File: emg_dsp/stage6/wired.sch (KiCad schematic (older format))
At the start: 51 parts, among them U38 OMNETICS_36, U41 MIC5365, U42 TC1016, U43 TC1016, U44 AD7980, U45 AD7980, U46 ADR381, U47 8X100, U48 8X100, U49 TC1016, U50 IL715-3, U51 DCP01DB, U52 IL715-3, U92 RHA2116, U93 RHA2116

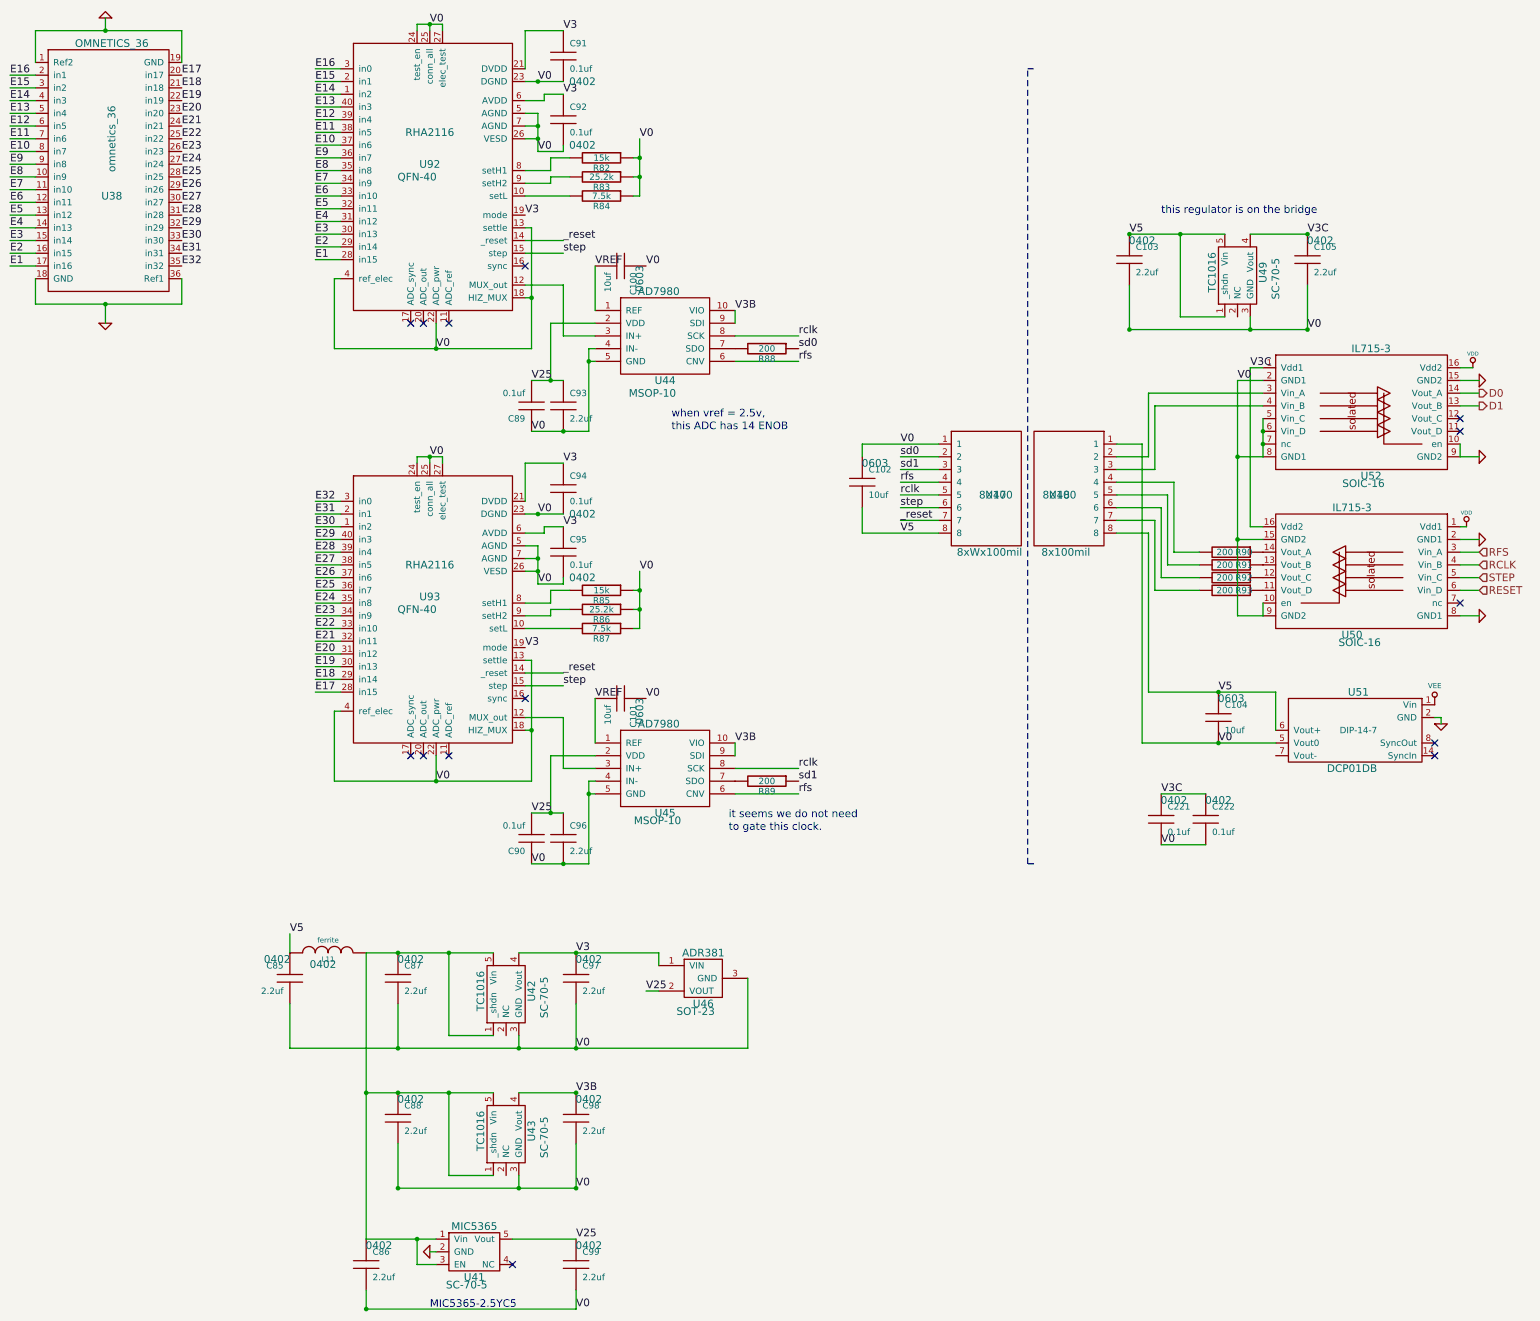
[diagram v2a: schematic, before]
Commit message: wired, wireless, some of bridge are routed. next up is the EMG system.
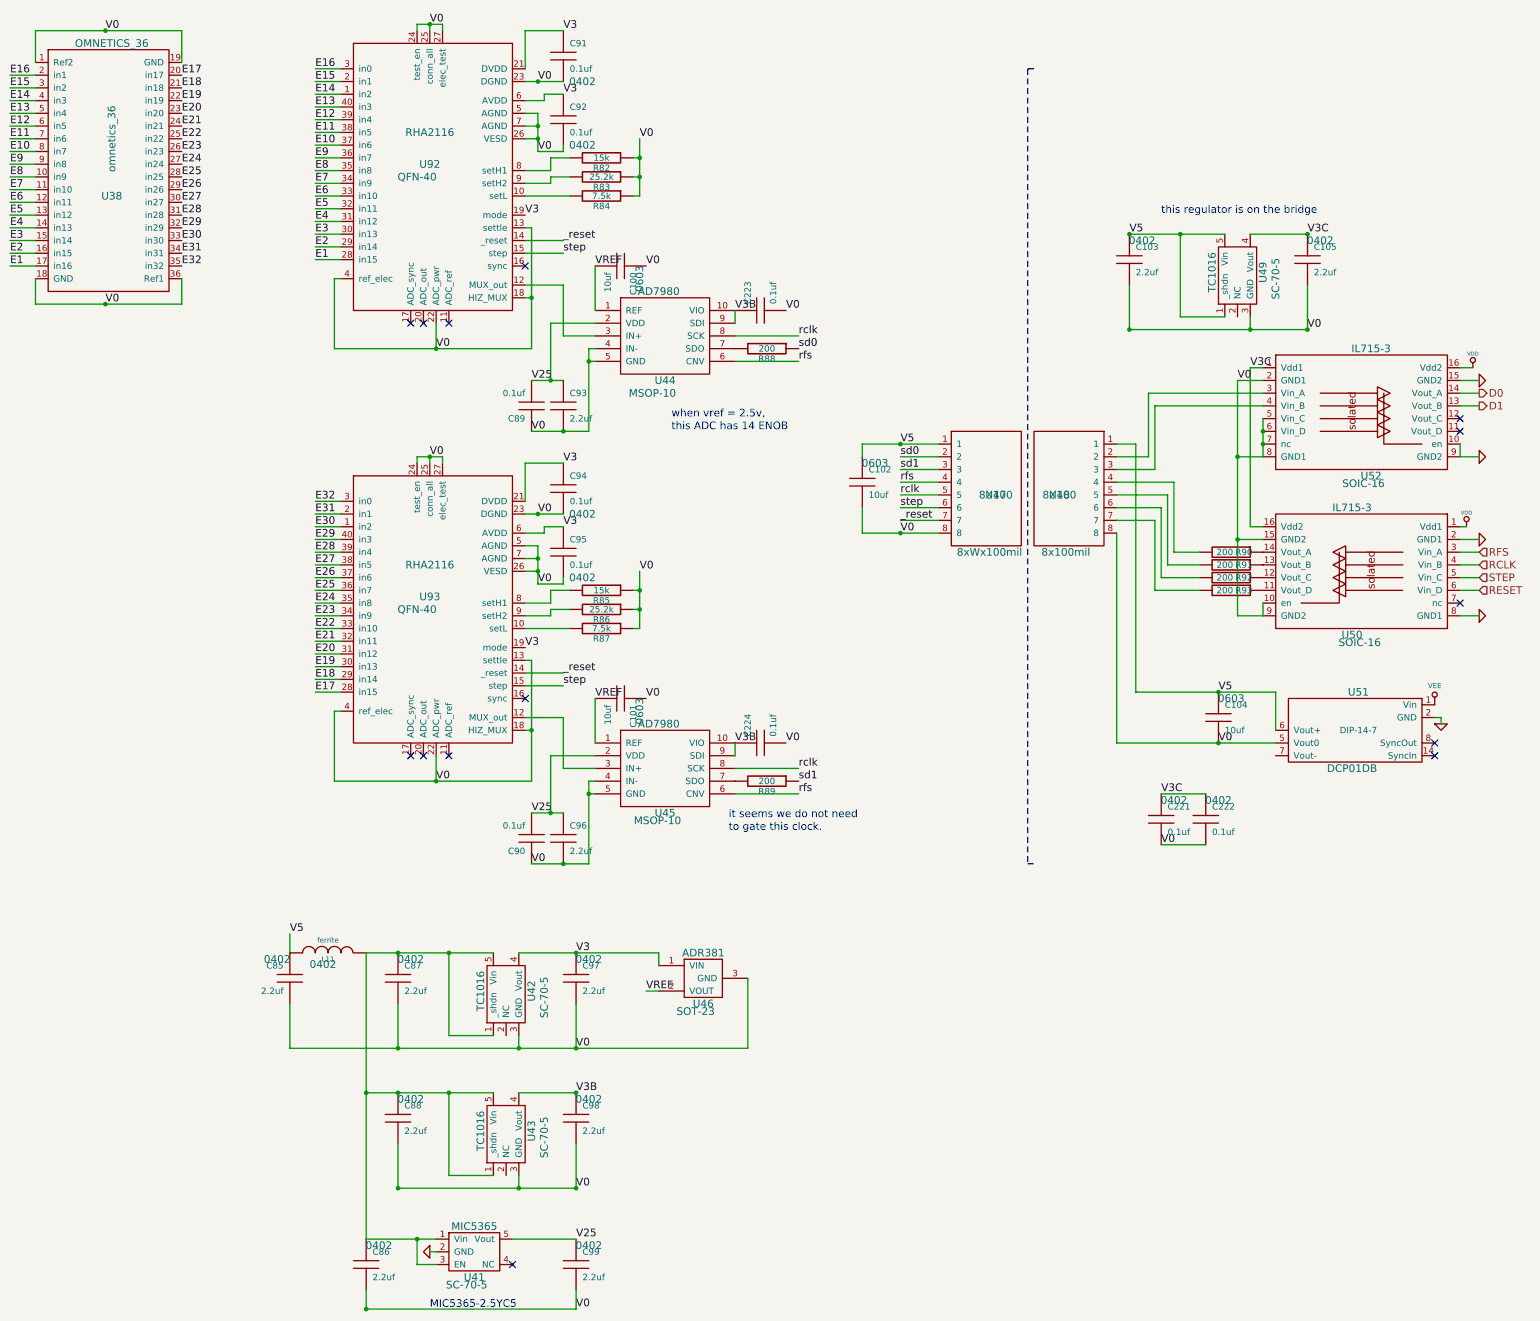
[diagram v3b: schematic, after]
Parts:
- added C223, C224: 0.1uf, 0402, symbol C
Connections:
- net GND: no longer U38.1 (Ref2), U38.18 (GND), U38.19 (GND), U38.36 (Ref1)
- net V0: now also C102.2, U38.1 (Ref2), U38.18 (GND), U38.19 (GND), U38.36 (Ref1), U47.8, U48.8, C223.2, C224.2; no longer C102.1, U47.1, U48.1
- net V25: no longer U46.2 (VOUT)
- net V3B: now also C223.1, C224.1
- net V5: now also C102.1, U47.1, U48.1; no longer C102.2, U47.8, U48.8
- net VREF: now also U46.2 (VOUT)

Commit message: getting closer -- needt o put DACs on the board so we can listen to the emg / neural data!
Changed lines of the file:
@@
-EESchema Schematic File Version 2  date Wed 29 Sep 2010 05:47:59 PM EDT
+EESchema Schematic File Version 2  date Thu 30 Sep 2010 12:31:09 AM EDT
 LIBS:power
 LIBS:device
@@
 Sheet 11 13
 Title "Stage 4 / Copyright 2010 Timothy L Hanson "
-Date "29 sep 2010"
+Date "30 sep 2010"
 Rev ""
 Comp "This design is free: redistribute or modify under the GPL v. 3 or later"
@@
 $EndDescr
 Wire Wire Line
-	9500 6400 9500 4750
+	9500 4750 9500 6400
 Wire Wire Line
-	10750 6400 9500 6400
+	9500 6400 10750 6400
 Wire Wire Line
 	9850 6800 10200 6800

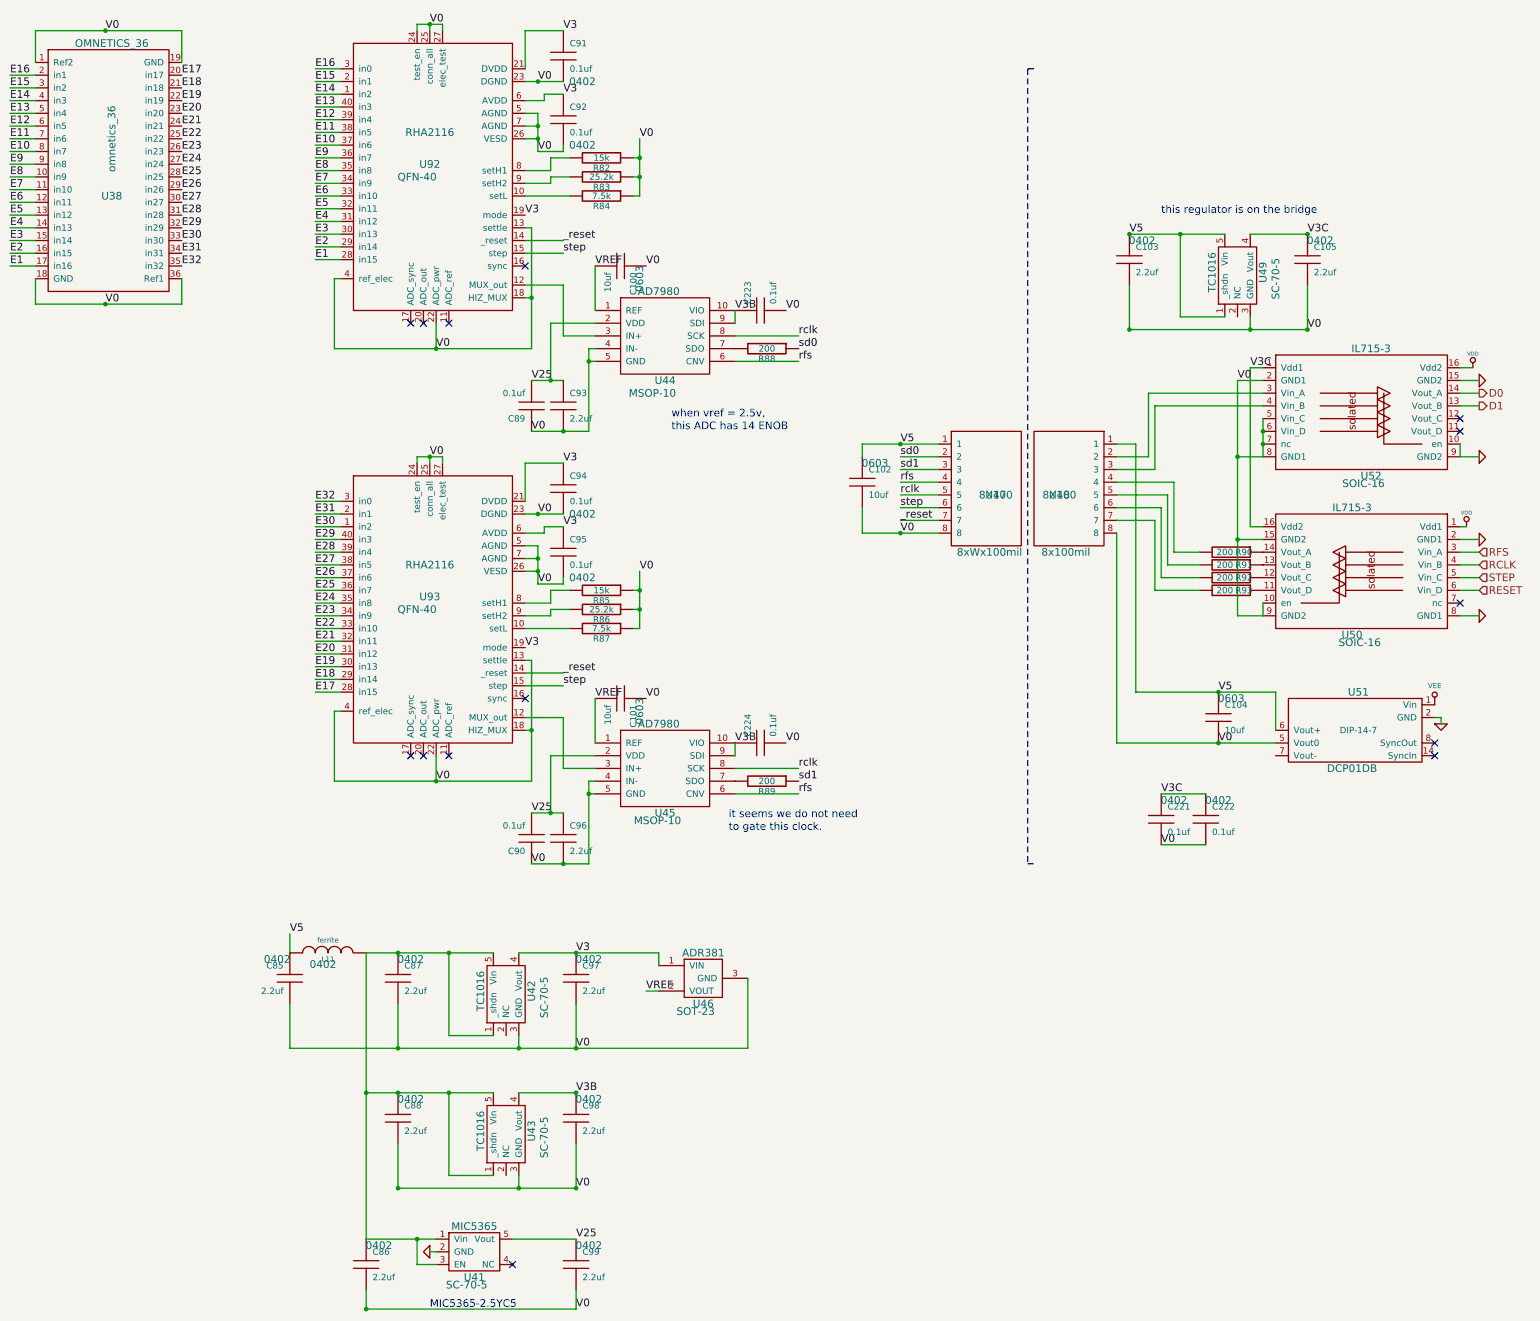
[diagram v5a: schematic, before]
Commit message: submitted a (partial) BOM .. !! board is not yet cone, but at least we now know to switch the footprint on the flash.
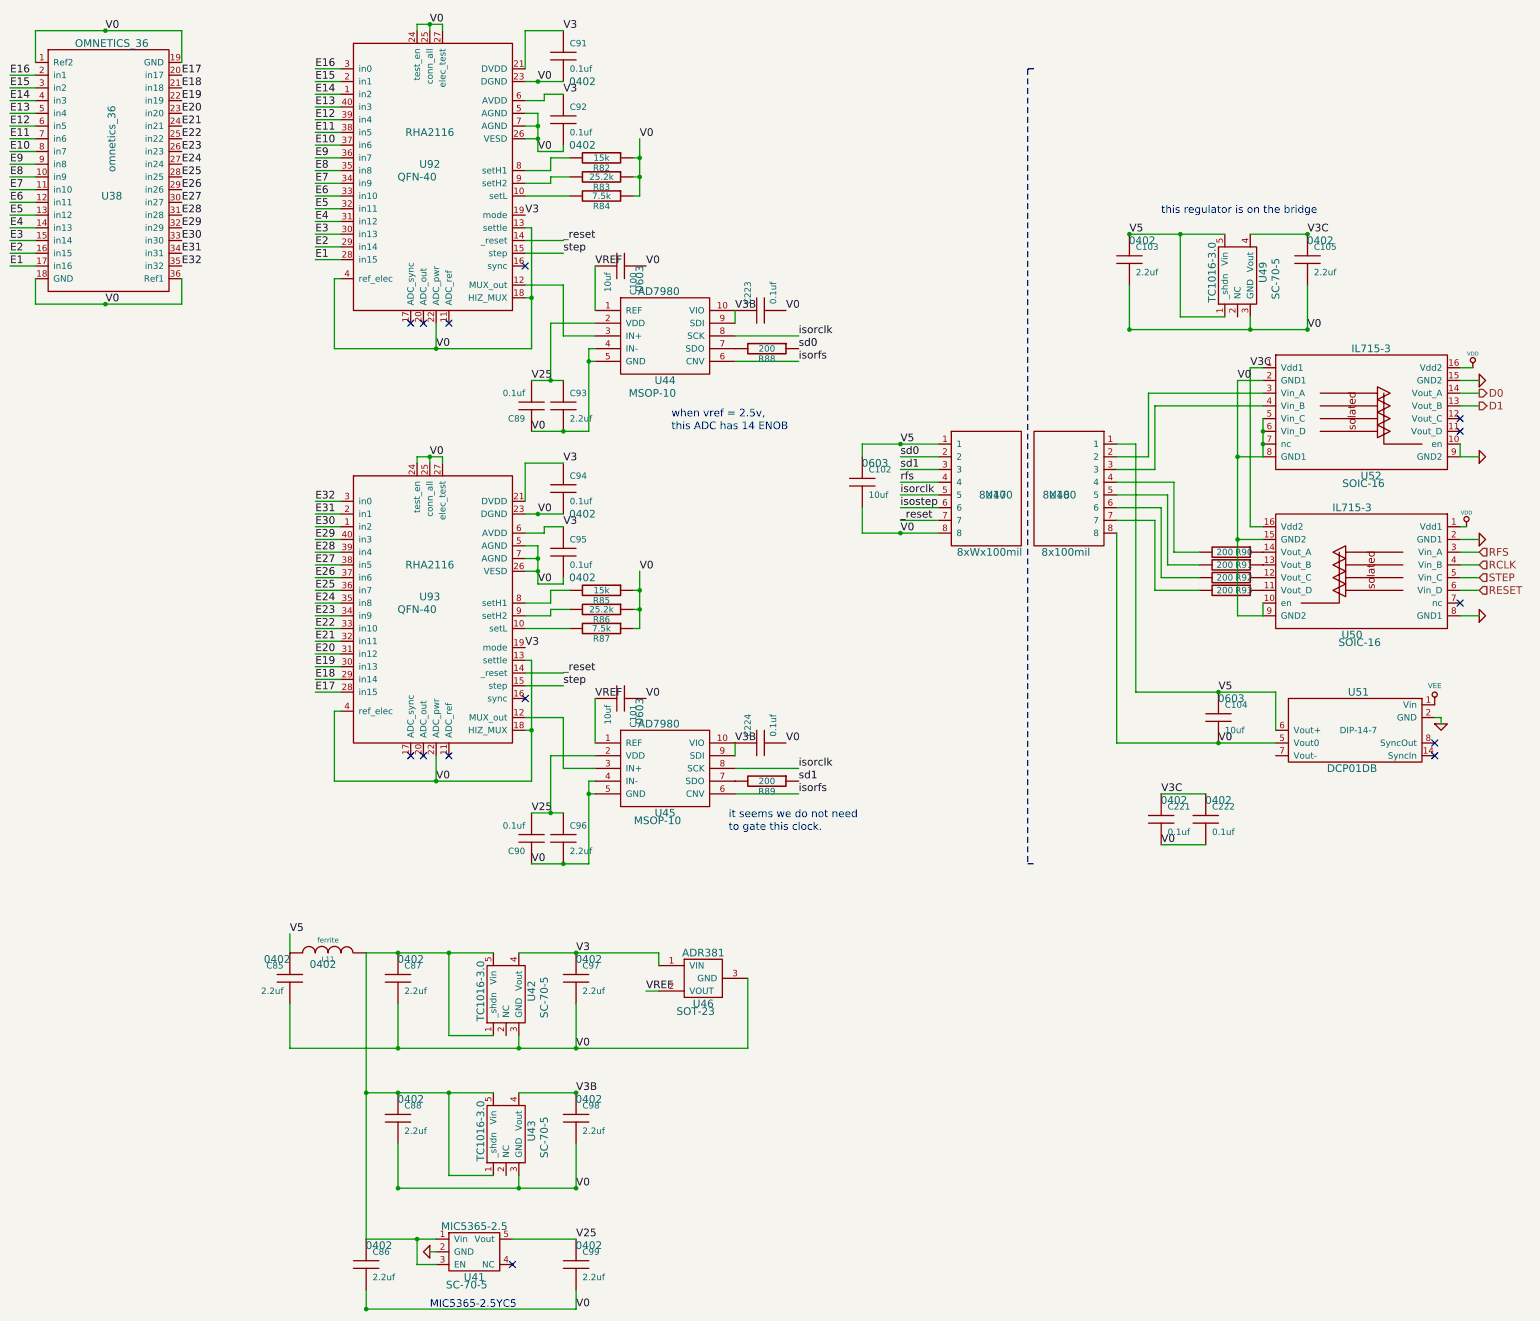
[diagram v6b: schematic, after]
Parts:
- U41: value MIC5365 -> MIC5365-2.5
- U42, U43, U49: value TC1016 -> TC1016-3.0
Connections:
- net rfs: no longer U44.6 (CNV), U45.6 (CNV)
- net step: no longer U47.6
- net rclk renamed isorclk
- new net isorfs: U44.6 (CNV), U45.6 (CNV)
- new net isostep: U47.6
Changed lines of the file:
@@
-EESchema Schematic File Version 2  date Thu 30 Sep 2010 05:10:58 PM EDT
+EESchema Schematic File Version 2  date Thu 30 Sep 2010 11:24:56 PM EDT
 LIBS:power
 LIBS:device
@@
 EELAYER END
 $Descr User 16000 12000
-Sheet 12 15
+Sheet 13 15
 Title "Stage 4 / Copyright 2010 Timothy L Hanson "
-Date "30 sep 2010"
+Date "1 oct 2010"
 Rev ""
 Comp "This design is free: redistribute or modify under the GPL v. 3 or later"
@@
 P 4700 9450
 F 0 "U43" H 4700 9250 60  0000 C CNN
-F 1 "TC1016" H 4700 9650 60  0000 C CNN
+F 1 "TC1016-3.0" H 4700 9650 60  0000 C CNN
 F 2 "SC-70-5" H 4650 9150 60  0000 C CNN
 	1    4700 9450
@@
 NoConn ~ 12200 3850
 $Comp
-L GND #PWR0300
+L GND #PWR0302
 U 1 1 4C9B921B
 P 12350 4800
-F 0 "#PWR0300" H 12350 4800 30  0001 C CNN
+F 0 "#PWR0302" H 12350 4800 30  0001 C CNN
 F 1 "GND" H 12350 4730 30  0001 C CNN
 	1    12350 4800
@@
 $EndComp
 $Comp
-L VDD #PWR0301
+L VDD #PWR0303
 U 1 1 4C9B9218
 P 12250 4700
-F 0 "#PWR0301" H 12250 4800 30  0001 C CNN
+F 0 "#PWR0303" H 12250 4800 30  0001 C CNN
 F 1 "VDD" H 12250 4810 30  0000 C CNN
 	1    12250 4700
@@
 $EndComp
 $Comp
-L GND #PWR0302
+L GND #PWR0304
 U 1 1 4C9B9215
 P 12350 5400
-F 0 "#PWR0302" H 12350 5400 30  0001 C CNN
+F 0 "#PWR0304" H 12350 5400 30  0001 C CNN
 F 1 "GND" H 12350 5330 30  0001 C CNN
 	1    12350 5400
@@
 $EndComp
 $Comp
-L GND #PWR0303
+L GND #PWR0305
 U 1 1 4C9B9212
 P 12350 4150
-F 0 "#PWR0303" H 12350 4150 30  0001 C CNN
+F 0 "#PWR0305" H 12350 4150 30  0001 C CNN
 F 1 "GND" H 12350 4080 30  0001 C CNN
 	1    12350 4150
@@
 $EndComp
 $Comp
-L GND #PWR0304
+L GND #PWR0306
 U 1 1 4C9B920A
 P 12350 3550
-F 0 "#PWR0304" H 12350 3550 30  0001 C CNN
+F 0 "#PWR0306" H 12350 3550 30  0001 C CNN
 F 1 "GND" H 12350 3480 30  0001 C CNN
 	1    12350 3550
@@
 $EndComp
 $Comp
-L VDD #PWR0305
+L VDD #PWR0307
 U 1 1 4C9B9204
 P 12300 3450
-F 0 "#PWR0305" H 12300 3550 30  0001 C CNN
+F 0 "#PWR0307" H 12300 3550 30  0001 C CNN
 F 1 "VDD" H 12300 3560 30  0000 C CNN
 	1    12300 3450
@@
 P 10450 2700
 F 0 "U49" H 10450 2500 60  0000 C CNN
-F 1 "TC1016" H 10450 2900 60  0000 C CNN
+F 1 "TC1016-3.0" H 10450 2900 60  0000 C CNN
 F 2 "SC-70-5" H 10400 2400 60  0000 C CNN
 	1    10450 2700
@@
 V0
 Text Label 7000 6600 0    60   ~ 0
-rclk
+isorclk
 Text Label 7000 6800 0    60   ~ 0
-rfs
+isorfs
 Text Label 7000 3400 0    60   ~ 0
-rfs
+isorfs
 Text Label 7000 3200 0    60   ~ 0
-rclk
+isorclk
 Text Label 7800 4450 0    60   ~ 0
-rclk
+isorclk
 Text Label 7800 4350 0    60   ~ 0
 rfs
@@
 _reset
 Text Label 7800 4550 0    60   ~ 0
-step
+isostep
 Text Label 7800 4050 0    60   ~ 0
 V5
@@
 $EndComp
 $Comp
-L GND #PWR0306
+L GND #PWR0308
 U 1 1 4C9B8790
 P 12050 6250
-F 0 "#PWR0306" H 12050 6250 30  0001 C CNN
+F 0 "#PWR0308" H 12050 6250 30  0001 C CNN
 F 1 "GND" H 12050 6180 30  0001 C CNN
 	1    12050 6250
@@
 P 4450 10400
 F 0 "U41" H 4450 10200 60  0000 C CNN
-F 1 "MIC5365" H 4450 10600 60  0000 C CNN
+F 1 "MIC5365-2.5" H 4450 10600 60  0000 C CNN
 F 2 "SC-70-5" H 4390 10140 60  0000 C CNN
 	1    4450 10400
@@
 $EndComp
 $Comp
-L GND #PWR0307
+L GND #PWR0309
 U 1 1 4CA0ED85
 P 4100 10400
-F 0 "#PWR0307" H 4100 10400 30  0001 C CNN
+F 0 "#PWR0309" H 4100 10400 30  0001 C CNN
 F 1 "GND" H 4100 10330 30  0001 C CNN
 	1    4100 10400
@@
 P 4700 8350
 F 0 "U42" H 4700 8150 60  0000 C CNN
-F 1 "TC1016" H 4700 8550 60  0000 C CNN
+F 1 "TC1016-3.0" H 4700 8550 60  0000 C CNN
 F 2 "SC-70-5" H 4650 8050 60  0000 C CNN
 	1    4700 8350
